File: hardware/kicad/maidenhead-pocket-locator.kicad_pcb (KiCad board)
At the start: 2 copper layers, 81 x 37 mm, 99 parts, among them J1 USB4105-GF-A, J2 JST-PH-3 BAT/NTC/GND, J3 WH1602B 1x16 LCD, J4 Hirose 20449-001E u.FL, Q1 DMP3098L P-MOS, Q2 DMN2050L N-MOS, Q3 DMN2050L backlight, Q4 DMP3098L BAT sense, Q5 DMN2050L BAT sense gate, SW1 LOCATE TL3305, SW2 OFF TL3305, SW3 BOOTSEL tact, SW4 RUN tact, U1 RP2040, U2 W25Q16JVUXIQ, U3 BQ24074RGTR, U4 TPS63802DLAR 3V3 buck-boost, U5 TPS61023DRLR LCD boost, U6 SN74LVC8T245PWR dual-rail, U7 Ai-Thinker GP-02 PROVISIONAL 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, U8 TPS22916 GNSS load switch, X1 12MHz crystal

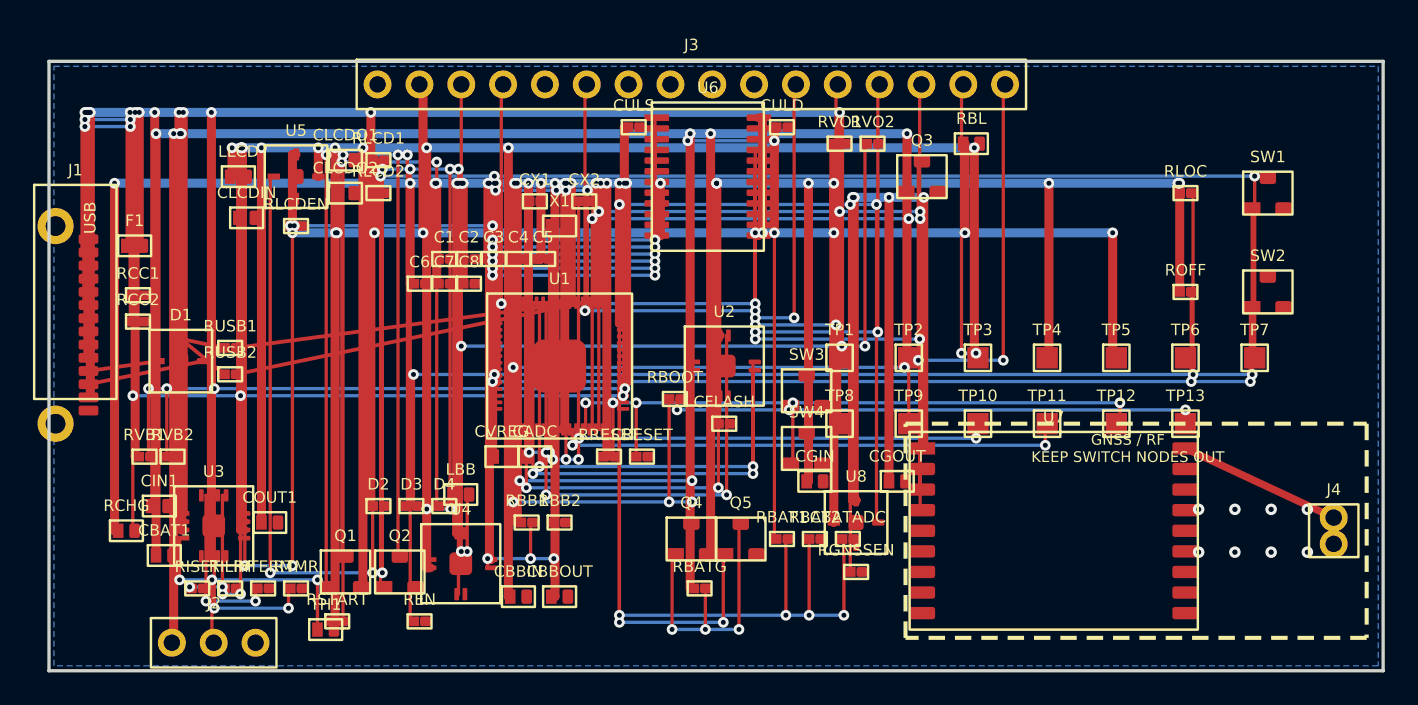
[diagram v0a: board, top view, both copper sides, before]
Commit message: Finish pocket locator project sources
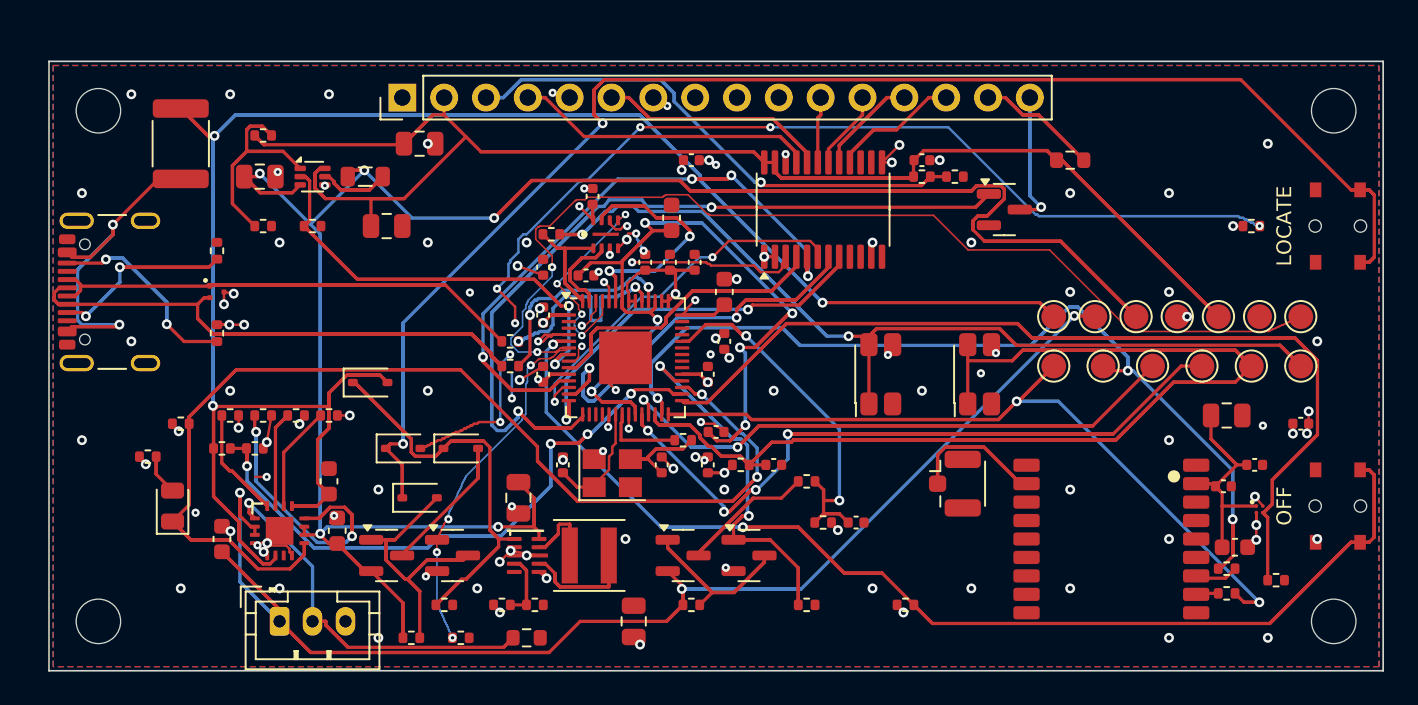
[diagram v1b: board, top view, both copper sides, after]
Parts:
- removed CADC: 1uF, RevA:CADC
- removed CBATADC: 100nF, RevA:CBATADC
- removed CBBIN: 10uF, RevA:CBBIN
- removed CBBOUT: 22uF, RevA:CBBOUT
- removed CFLASH: 100nF, RevA:CFLASH
- removed CGIN: 1uF, RevA:CGIN
- removed CGOUT: 4.7uF, RevA:CGOUT
- removed CLCDIN: 4.7uF, RevA:CLCDIN
- removed CRESET: 100nF, RevA:CRESET
- removed CULD: 100nF, RevA:CULD
- removed CULS: 100nF, RevA:CULS
- removed CVREG: 1uF, RevA:CVREG
- removed LBB: 0.47uH, RevA:LBB
- removed LLCD: 1uH, RevA:LLCD
- removed RBATG: 1M, RevA:RBATG
- removed RBL: 68R safe-start, RevA:RBL
- removed RBOOT: 1k, RevA:RBOOT
- removed RCHG: 1k, RevA:RCHG
- removed REN: 1M, RevA:REN
- removed RGNSSEN: 100k, RevA:RGNSSEN
- removed RILIM: 2.00k, RevA:RILIM
- removed RISET: 2.20k 404mA, RevA:RISET
- removed RITERM: 3.30k, RevA:RITERM
- removed RLCDEN: 100k, RevA:RLCDEN
- removed RLOC: 100k, RevA:RLOC
- removed ROFF: 100k, RevA:ROFF
- removed RRESET: 100k, RevA:RRESET
- removed RSTART: 1M, RevA:RSTART
- removed RTMR: 48.7k, RevA:RTMR
- added C9: 100nF, Capacitor_SMD:C_0402_1005Metric, F.Cu at (30.0, 12.5)
- added CADC1: 1uF, Capacitor_SMD:C_0603_1608Metric, F.Cu at (41.0, 14.0)
- added CBATADC1: 100nF, Capacitor_SMD:C_0402_1005Metric, F.Cu at (49.0, 28.0)
- added CBBIN1: 10uF, Capacitor_SMD:C_0805_2012Metric, F.Cu at (28.5, 26.5)
- added CBBOUT1: 22uF, Capacitor_SMD:C_0805_2012Metric, F.Cu at (35.5, 34.0)
- added CDV1: 100nF, Capacitor_SMD:C_0402_1005Metric, F.Cu at (40.5, 22.5)
- added CDV2: 100nF, Capacitor_SMD:C_0402_1005Metric, F.Cu at (32.6, 13.0)
- added CFLASH1: 100nF, Capacitor_SMD:C_0402_1005Metric, F.Cu at (33.0, 8.20)
- added CGIN1: 1uF, Capacitor_SMD:C_0402_1005Metric, F.Cu at (76.0, 22.0)
- added CGNSS1: 100nF, Capacitor_SMD:C_0402_1005Metric, F.Cu at (71.3, 25.8)
- added CGNSS2: 820pF, Capacitor_SMD:C_0402_1005Metric, F.Cu at (73.2, 24.5)
- added CGNSS3: 10uF, Capacitor_SMD:C_0805_2012Metric, F.Cu at (71.5, 21.5)
- added CGOUT1: 4.7uF, Capacitor_SMD:C_0603_1608Metric, F.Cu at (72.0, 29.5)
- added CLCDIN1: 10uF, Capacitor_SMD:C_0805_2012Metric, F.Cu at (12.8, 7.00)
- added CRESET1: 100nF, Capacitor_SMD:C_0402_1005Metric, F.Cu at (44.0, 24.5)
- added CULD1: 100nF, Capacitor_SMD:C_0402_1005Metric, F.Cu at (53.0, 6.00)
- added CULS1: 100nF, Capacitor_SMD:C_0402_1005Metric, F.Cu at (39.0, 6.00)
- added CVREG1: 1uF, Capacitor_SMD:C_0603_1608Metric, F.Cu at (37.8, 9.50)
- added D5: 1N4148WS, Diode_SMD:D_SOD-323, F.Cu at (21.5, 23.5)
- added H1: M2.5, MountingHole:MountingHole_2.7mm_M2.5, F.Cu at (3.00, 3.00)
- added H2: M2.5, MountingHole:MountingHole_2.7mm_M2.5, F.Cu at (78.0, 3.00)
- added H3: M2.5, MountingHole:MountingHole_2.7mm_M2.5, F.Cu at (3.00, 34.0)
- added H4: M2.5, MountingHole:MountingHole_2.7mm_M2.5, F.Cu at (78.0, 34.0)
- added LBB1: XFL4020-471MEC, Inductor_SMD:L_Coilcraft_XxL4020, F.Cu at (32.8, 30.0)
- added LED1: KP-2012EC, LED_SMD:LED_0805_2012Metric, F.Cu at (7.50, 27.0)
- added LLCD1: LQH2MCN1R0M02L, Inductor_SMD:L_0805_2012Metric, F.Cu at (19.2, 7.00)
- added RBATG1: 100k, Resistor_SMD:R_0402_1005Metric, F.Cu at (39.0, 33.0)
- added RBL1: 68R, Resistor_SMD:R_0603_1608Metric, F.Cu at (62.0, 6.00)
- added RBOOT1: 1k, Resistor_SMD:R_0402_1005Metric, F.Cu at (30.5, 10.5)
- added RCHG1: 1k, Resistor_SMD:R_0402_1005Metric, F.Cu at (6.00, 24.0)
- added RCHGPU1: 100k, Resistor_SMD:R_0402_1005Metric, F.Cu at (8.00, 22.0)
- added REN1: 1M, Resistor_SMD:R_0402_1005Metric, F.Cu at (24.0, 33.0)
- added RGNSSEN1: 100k, Resistor_SMD:R_0402_1005Metric, F.Cu at (74.5, 31.5)
- added RGNSSRX1: 33R, Resistor_SMD:R_0402_1005Metric, F.Cu at (71.5, 30.8)
- added RGNSSTX1: 33R, Resistor_SMD:R_0402_1005Metric, F.Cu at (71.5, 32.3)
- added RHOLD1: 100k, Resistor_SMD:R_0402_1005Metric, F.Cu at (25.0, 35.0)
- added RILIM1: 2.00k, Resistor_SMD:R_0402_1005Metric, F.Cu at (13.0, 21.5)
- added RISET1: 2.20k, Resistor_SMD:R_0402_1005Metric, F.Cu at (11.0, 21.5)
- added RITERM1: 3.30k, Resistor_SMD:R_0402_1005Metric, F.Cu at (15.0, 21.5)
- added RLCDEN1: 100k, Resistor_SMD:R_0402_1005Metric, F.Cu at (16.0, 10.0)
- added RLOC1: 100k, Resistor_SMD:R_0402_1005Metric, F.Cu at (73.0, 10.0)
- added ROFF1: 100k, Resistor_SMD:R_0402_1005Metric, F.Cu at (52.0, 33.0)
- added RRESET1: 100k, Resistor_SMD:R_0402_1005Metric, F.Cu at (42.0, 24.5)
- added RSENSEEN1: 100k, Resistor_SMD:R_0402_1005Metric, F.Cu at (46.0, 33.0)
- added RSTART1: 100k, Resistor_SMD:R_0402_1005Metric, F.Cu at (22.0, 35.0)
- added RTMR1: 48.7k, Resistor_SMD:R_0402_1005Metric, F.Cu at (17.0, 21.5)
- added RXTAL1: 1k, Resistor_SMD:R_0402_1005Metric, F.Cu at (38.5, 23.0)
- C1: footprint RevA:C1 -> Capacitor_SMD:C_0402_1005Metric
- C2: footprint RevA:C2 -> Capacitor_SMD:C_0402_1005Metric
- C3: footprint RevA:C3 -> Capacitor_SMD:C_0402_1005Metric
- C4: footprint RevA:C4 -> Capacitor_SMD:C_0402_1005Metric
- C5: footprint RevA:C5 -> Capacitor_SMD:C_0402_1005Metric
- C6: footprint RevA:C6 -> Capacitor_SMD:C_0402_1005Metric
- C7: footprint RevA:C7 -> Capacitor_SMD:C_0402_1005Metric
- C8: footprint RevA:C8 -> Capacitor_SMD:C_0402_1005Metric
- CBAT1: footprint RevA:CBAT1 -> Capacitor_SMD:C_0603_1608Metric
- CIN1: footprint RevA:CIN1 -> Capacitor_SMD:C_0603_1608Metric
- CLCDO1: footprint RevA:CLCDO1 -> Capacitor_SMD:C_0805_2012Metric
- CLCDO2: footprint RevA:CLCDO2 -> Capacitor_SMD:C_0805_2012Metric
- COUT1: footprint RevA:COUT1 -> Capacitor_SMD:C_0603_1608Metric
- CX1: value 12pF C0G -> 15pF; footprint RevA:CX1 -> Capacitor_SMD:C_0402_1005Metric
- CX2: value 12pF C0G -> 15pF; footprint RevA:CX2 -> Capacitor_SMD:C_0402_1005Metric
- D1: value USBLC6-2SC6 -> TPD2EUSB30DRTR; footprint RevA:D1 -> PocketLocator:Texas_DRT0003A
- D2: value BAT54 VBUS OR -> BAT54H; footprint RevA:D2 -> Diode_SMD:D_SOD-323
- D3: value BAT54 LOCATE isolate -> 1N4148WS; footprint RevA:D3 -> Diode_SMD:D_SOD-323
- D4: value BAT54 START OR -> BAT54H; footprint RevA:D4 -> Diode_SMD:D_SOD-323
- F1: value 500mA PTC -> MF-MSMF050-2; footprint RevA:F1 -> Fuse:Fuse_1812_4532Metric
- J1: footprint RevA:J1 -> PocketLocator:USB4105-GF-A
- J2: value JST-PH-3 BAT/NTC/GND -> B3B-PH-K-S(LF)(SN); footprint RevA:J2 -> Connector_JST:JST_PH_B3B-PH-K_1x03_P2.00mm_Vertical
- J3: value WH1602B 1x16 LCD -> 61301611121; footprint RevA:J3 -> Connector_PinHeader_2.54mm:PinHeader_1x16_P2.54mm_Vertical
- J4: value Hirose 20449-001E u.FL -> Hirose 20449-001E; footprint RevA:J4 -> Connector_Coaxial:U.FL_Hirose_U.FL-R-SMT-1_Vertical
- Q1: value DMP3098L P-MOS -> DMP3098L-7; footprint RevA:Q1 -> Package_TO_SOT_SMD:SOT-23
- Q2: value DMN2050L N-MOS -> DMN2050L-7; footprint RevA:Q2 -> Package_TO_SOT_SMD:SOT-23
- Q3: value DMN2050L backlight -> DMN2050L-7; footprint RevA:Q3 -> Package_TO_SOT_SMD:SOT-23
- Q4: value DMP3098L BAT sense -> DMP3098L-7; footprint RevA:Q4 -> Package_TO_SOT_SMD:SOT-23
- Q5: value DMN2050L BAT sense gate -> DMN2050L-7; footprint RevA:Q5 -> Package_TO_SOT_SMD:SOT-23
- RBAT1: footprint RevA:RBAT1 -> Resistor_SMD:R_0402_1005Metric
- RBAT2: footprint RevA:RBAT2 -> Resistor_SMD:R_0402_1005Metric
- RBB1: footprint RevA:RBB1 -> Resistor_SMD:R_0402_1005Metric
- RBB2: footprint RevA:RBB2 -> Resistor_SMD:R_0402_1005Metric
- RCC1: footprint RevA:RCC1 -> Resistor_SMD:R_0402_1005Metric
- RCC2: value 5.4k -> 5.1k; footprint RevA:RCC2 -> Resistor_SMD:R_0402_1005Metric
- RLCD1: value 732k -> 909k; footprint RevA:RLCD1 -> Resistor_SMD:R_0402_1005Metric
- RLCD2: footprint RevA:RLCD2 -> Resistor_SMD:R_0402_1005Metric
- RUSB1: footprint RevA:RUSB1 -> Resistor_SMD:R_0402_1005Metric
- RUSB2: footprint RevA:RUSB2 -> Resistor_SMD:R_0402_1005Metric
- RVB1: value 150k -> 82k; footprint RevA:RVB1 -> Resistor_SMD:R_0402_1005Metric
- RVB2: footprint RevA:RVB2 -> Resistor_SMD:R_0402_1005Metric
- RVO1: footprint RevA:RVO1 -> Resistor_SMD:R_0402_1005Metric
- RVO2: footprint RevA:RVO2 -> Resistor_SMD:R_0402_1005Metric
- SW1: value LOCATE TL3305 -> TL1014BF160QG; footprint RevA:SW1 -> PocketLocator:SW_TL1014B
- SW2: value OFF TL3305 -> TL1014BF160QG; footprint RevA:SW2 -> PocketLocator:SW_TL1014B
- SW3: value BOOTSEL tact -> EVQ-P7A01P; footprint RevA:SW3 -> Button_Switch_SMD:SW_SPST_EVQP7A
- SW4: value RUN tact -> EVQ-P7A01P; footprint RevA:SW4 -> Button_Switch_SMD:SW_SPST_EVQP7A
- TH1: footprint RevA:TH1 -> Resistor_SMD:R_0603_1608Metric
- TP1: footprint RevA:TP1 -> TestPoint:TestPoint_Pad_D1.5mm
- TP10: footprint RevA:TP10 -> TestPoint:TestPoint_Pad_D1.5mm
- TP11: footprint RevA:TP11 -> TestPoint:TestPoint_Pad_D1.5mm
- TP12: footprint RevA:TP12 -> TestPoint:TestPoint_Pad_D1.5mm
- TP13: footprint RevA:TP13 -> TestPoint:TestPoint_Pad_D1.5mm
- TP2: footprint RevA:TP2 -> TestPoint:TestPoint_Pad_D1.5mm
- TP3: footprint RevA:TP3 -> TestPoint:TestPoint_Pad_D1.5mm
- TP4: footprint RevA:TP4 -> TestPoint:TestPoint_Pad_D1.5mm
- TP5: footprint RevA:TP5 -> TestPoint:TestPoint_Pad_D1.5mm
- TP6: footprint RevA:TP6 -> TestPoint:TestPoint_Pad_D1.5mm
- TP7: footprint RevA:TP7 -> TestPoint:TestPoint_Pad_D1.5mm
- TP8: footprint RevA:TP8 -> TestPoint:TestPoint_Pad_D1.5mm
- TP9: footprint RevA:TP9 -> TestPoint:TestPoint_Pad_D1.5mm
- U1: footprint RevA:U1 -> Package_DFN_QFN:QFN-56-1EP_7x7mm_P0.4mm_EP3.2x3.2mm
- U2: footprint RevA:U2 -> PocketLocator:Winbond_UX_8
- U3: footprint RevA:U3 -> PocketLocator:Texas_RGT0016C
- U4: value TPS63802DLAR 3V3 buck-boost -> TPS63802DLAR; footprint RevA:U4 -> PocketLocator:Texas_DLA0010A
- U5: value TPS61023DRLR LCD boost -> TPS61023DRLR; footprint RevA:U5 -> Package_TO_SOT_SMD:SOT-563
- U6: value SN74LVC8T245PWR dual-rail -> SN74LVC8T245PWR; footprint RevA:U6 -> Package_SO:TSSOP-24_4.4x7.8mm_P0.65mm
- U7: value Ai-Thinker GP-02 PROVISIONAL FOOTPRINT -> Ai-Thinker GP-02; footprint RevA:U7 -> PocketLocator:GP-02
- U8: value TPS22916 GNSS load switch -> TPS22916BYFPR; footprint RevA:U8 -> PocketLocator:Texas_YFP0004
- X1: value 12MHz crystal -> ABM8-272-T3; footprint RevA:X1 -> Crystal:Crystal_SMD_Abracon_ABM8G-4Pin_3.2x2.5mm
- moved U8 24.5 mm to (73.5, 27.2)
- moved J4 23.2 mm to (55.0, 25.6)
- moved C3 18.0 mm to (40.0, 24.5), turned to 90 degrees
- moved J3 17.6 mm to (21.4, 2.20), turned to 90 degrees
- moved RUSB2 17.0 mm to (28.0, 18.5)
- moved RUSB1 17.0 mm to (28.0, 17.0)
- moved C6 16.8 mm to (39.2, 12.2), turned to 90 degrees
- moved CX2 16.7 mm to (37.2, 24.5), turned to 90 degrees
- moved CX1 16.1 mm to (31.2, 24.5), turned to 90 degrees
- moved X1 15.3 mm to (34.2, 25.0)
- moved C7 13.8 mm to (37.7, 12.2), turned to 90 degrees
- moved SW2 13.7 mm to (78.2, 27.0), turned to -90 degrees
- moved C4 13.5 mm to (40.0, 19.0), turned to 90 degrees
- moved TP8 13.5 mm to (61.0, 18.5)
- moved TP1 13.2 mm to (61.0, 15.5)
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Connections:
- CX2 pad 1: XOUT -> XOUT_XTAL
- D1 pad 2: GND -> USB_DM_CONN
- D1 pad 3: USB_DM_CONN -> GND
- D2 pad 1: VBUS -> PWR_EN
- D2 pad 2: PWR_EN -> VBUS
- D3 pad 1: PWR_START_GATE -> LOCATE_RAW
- D3 pad 2: LOCATE_N -> PWR_START_GATE
- D4 pad 1: PWR_START_OUT -> PWR_EN
- D4 pad 2: PWR_EN -> PWR_START_OUT
- F1 pad 1: VBUS -> VBUS_RAW
- J1 pad A4: VBUS -> VBUS_RAW
- J1 pad A9: VBUS -> VBUS_RAW
- J1 pad B4: VBUS -> VBUS_RAW
- J1 pad B9: VBUS -> VBUS_RAW
- RUSB1 pad 1: USB_DP_ESD -> USB_DP_CONN
- RUSB2 pad 1: USB_DM_ESD -> USB_DM_CONN
- SW1 pad 1: LOCATE_N -> LOCATE_RAW
- SW1 pad 3: (no net) -> LOCATE_RAW
- SW2 pad 3: (no net) -> OFF_N
- U2 pad 9: GND -> (no net)
- U3 pad 1: VBUS -> CHG_TS
- U3 pad 13: CHG_ISET -> VBUS
- U3 pad 14: VBUS_PRESENT -> CHG_TMR
- U3 pad 16: GND -> CHG_ISET
- U3 pad 4: CHG_TS -> GND
- U3 pad 7: CHG_TMR -> (no net)
- U4 pad 1: BB_SW1 -> PWR_EN
- U4 pad 10: 3V3 -> SYS_RAW
- U4 pad 2: SYS_RAW -> GND
- U4 pad 3: PWR_EN -> GND
- U4 pad 4: GND -> BB_FB
- U4 pad 5: BB_FB -> (no net)
- U4 pad 8: 3V3 -> GND
- U4 pad 9: GND -> BB_SW1
- U6 pad 1: LCD_RS_3V3 -> 3V3
- U6 pad 12: 3V3 -> GND
- U6 pad 13: 5V_LCD -> GND
- U6 pad 2: LCD_E_3V3 -> 3V3
- U6 pad 22: (no net) -> GND
- U6 pad 23: GND -> 5V_LCD
- U6 pad 3: LCD_D4_3V3 -> LCD_RS_3V3
- U6 pad 4: LCD_D5_3V3 -> LCD_E_3V3
- U6 pad 5: LCD_D6_3V3 -> LCD_D4_3V3
- U6 pad 6: LCD_D7_3V3 -> LCD_D5_3V3
- U6 pad 7: (no net) -> LCD_D6_3V3
- U6 pad 8: (no net) -> LCD_D7_3V3
- U7 pad 1: 3V3_GNSS -> GND
- U7 pad 10: (no net) -> GND
- U7 pad 11: (no net) -> GNSS_RF_50R
- U7 pad 12: (no net) -> GND
- U7 pad 17: GND -> (no net)
- U7 pad 18: GNSS_RF_50R -> (no net)
- U7 pad 2: GND -> GNSS_TX_U7
- U7 pad 3: GNSS_TX -> GNSS_RX_U7
- U7 pad 4: GNSS_RX -> GNSS_PPS
- U7 pad 5: GNSS_PPS -> (no net)
- U7 pad 8: (no net) -> 3V3_GNSS
- X1 pad 2: XOUT -> GND
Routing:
- net 3V3: track 447.8 -> 43.1 mm, vias 34 -> 22
- net LOCATE_RAW: track 0.00 -> 140.6 mm, vias 0 -> 2
- net BAT: track 217.5 -> 115.4 mm, vias 7 -> 3
- net PWR_START_GATE: track 105.7 -> 24.5 mm, vias 4 -> 0
- net VBUS: track 263.9 -> 191.6 mm, vias 13 -> 3
- net RUN_N: track 46.2 -> 116.7 mm, vias 5 -> 0
- net CHG_N: track 46.9 -> 112.0 mm, vias 3 -> 2
- net USB_DM_CONN: track 12.7 -> 75.7 mm
- net LCD_FB: track 79.3 -> 19.8 mm, vias 3 -> 0
- net PWR_EN: track 99.3 -> 40.2 mm, vias 4 -> 0
- net 3V3_GNSS: track 74.0 -> 17.1 mm, vias 4 -> 0
- net SYS_RAW: track 244.0 -> 196.2 mm, vias 11 -> 5
- net BOOTSEL_N: track 32.9 -> 79.6 mm, vias 3 -> 2
- net LCD_SW: track 51.8 -> 8.07 mm, vias 2 -> 0
- net PWR_START_OUT: track 50.9 -> 10.3 mm, vias 2 -> 0
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- added copper zone on In2.Cu, net 3V3
- added copper zone on F.Cu, net GND
- added copper zone on In1.Cu, net GND
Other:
- copper layers 2 -> 4
- board text added: "LOCATE"
- board text added: "OFF"
- board text removed: "GNSS / RF KEEP SWITCH NODES OUT"
- board text removed: "USB"
